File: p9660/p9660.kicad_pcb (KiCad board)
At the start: 2 copper layers, 58 x 51 mm, 6 parts, among them J1 Conn_02x08_Counter_Clockwise, J2 Conn_02x08_Counter_Clockwise, J3 Conn_02x08_Counter_Clockwise, J4 Conn_02x08_Counter_Clockwise, J5 Conn_02x04_Counter_Clockwise

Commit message: done for realz?
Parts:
- added REF**: balls, Hayden Crimes:balls, B.Cu at (70.4, 47.7)
- added TP1: TestPoint, TestPoint:TestPoint_Pad_2.0x2.0mm, F.Cu at (42.0, 31.0)
- added TP2: TestPoint, TestPoint:TestPoint_Pad_2.0x2.0mm, F.Cu at (42.0, 78.0)
- added TP3: TestPoint, TestPoint:TestPoint_Pad_2.0x2.0mm, F.Cu at (96.0, 78.0)
- added TP4: TestPoint, TestPoint:TestPoint_Pad_2.0x2.0mm, F.Cu at (96.0, 31.0)
- added TP5: TestPoint, TestPoint:TestPoint_Pad_2.0x2.0mm, F.Cu at (63.0, 31.0)
- added TP6: TestPoint, TestPoint:TestPoint_Pad_2.0x2.0mm, F.Cu at (62.0, 78.0)
- added TP7: TestPoint, TestPoint:TestPoint_Pad_2.0x2.0mm, F.Cu at (75.0, 31.0)
- added TP8: TestPoint, TestPoint:TestPoint_Pad_2.0x2.0mm, F.Cu at (76.0, 78.0)
- moved J5 2.04 mm to (73.0, 75.5)
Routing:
- net CK1-: track 36.2 -> 38.2 mm
- net CK1+: track 36.3 -> 38.3 mm
- net CK2+: track 24.2 -> 26.3 mm
- net CK2-: track 24.3 -> 26.4 mm
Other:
- board text added: "github.com/hadn69/P9660-Breakout"

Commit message: Update p9660.kicad_pcb
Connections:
- C1 pad 3: D3 -> GND
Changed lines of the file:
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@@
 		)
 		(property "Value" "~"
-			(at -3 2 270)
+			(at -3 2 -90)
 			(unlocked yes)
 			(layer "F.Fab")
@@
 			(layer "F.SilkS")
 		)
-		(pad "1" thru_hole circle
-			(at 1.045 0.63 270)
-			(size 1.22 1.22)
-			(drill 0.71)
-			(layers "*.Cu" "*.Mask")
-			(remove_unused_layers no)
-			(net 2 "GND")
-			(pinfunction "GND")
-			(pintype "input")
-		)
-		(pad "1" thru_hole circle
+		(pad "" np_thru_hole circle
 			(at 1.045 2.35 270)
 			(size 0.84 0.84)
 			(drill 0.84)
-			(property pad_prop_heatsink)
-			(layers "*.Cu" "*.Mask")
-			(remove_unused_layers no)
+			(layers "F&B.Cu" "*.Mask")
 			(pinfunction "GND")
 			(pintype "input")
@@
 				(prefer_zone_connections no)
 			)
+		)
+		(pad "1" thru_hole circle
+			(at 1.045 0.63 270)
+			(size 1.22 1.22)
+			(drill 0.71)
+			(layers "*.Cu" "*.Mask")
+			(remove_unused_layers no)
+			(net 2 "GND")
+			(pinfunction "GND")
+			(pintype "input")
 		)
 		(pad "1" smd oval
@@
 			(property pad_prop_bga)
 			(layers "F.Cu" "F.Paste" "F.Mask")
-			(net 13 "D3")
+			(net 2 "GND")
 			(pinfunction "D3")
 			(pintype "input")

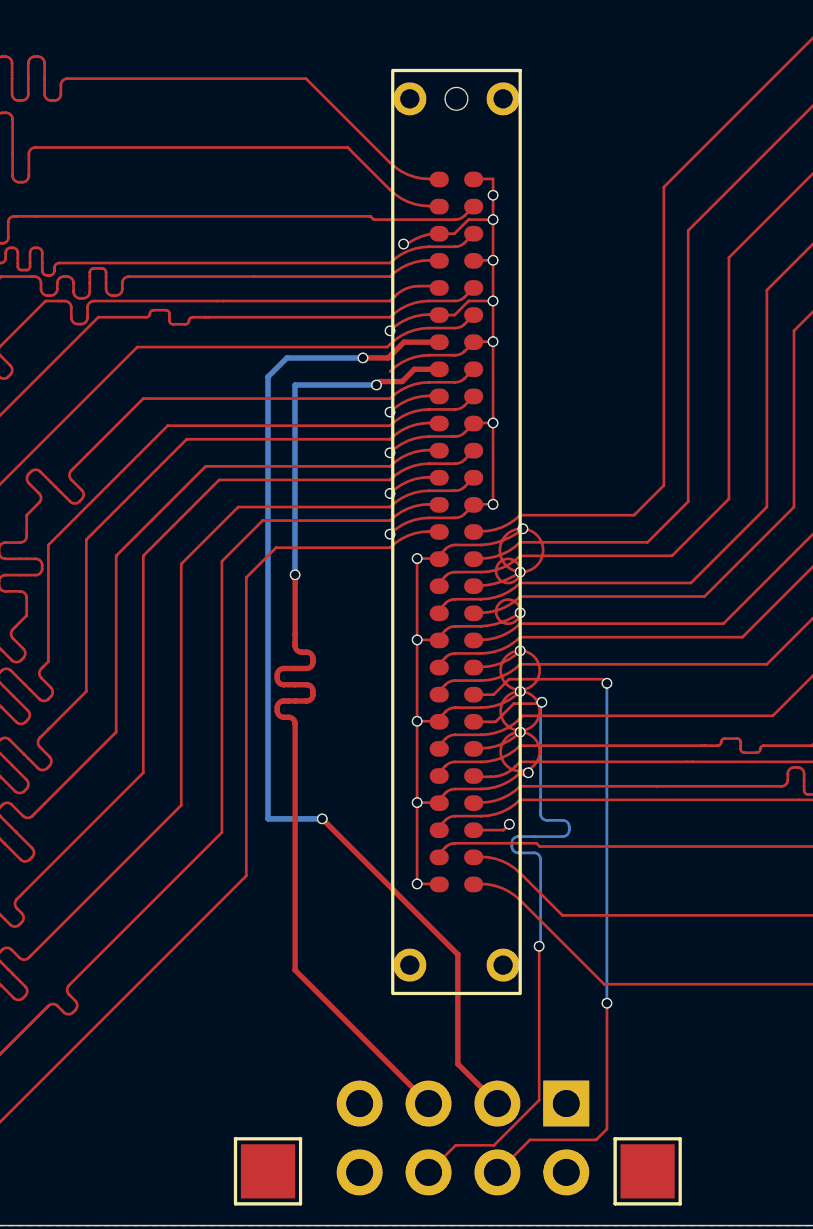
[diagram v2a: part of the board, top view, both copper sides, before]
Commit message: added renders + followed keepout better
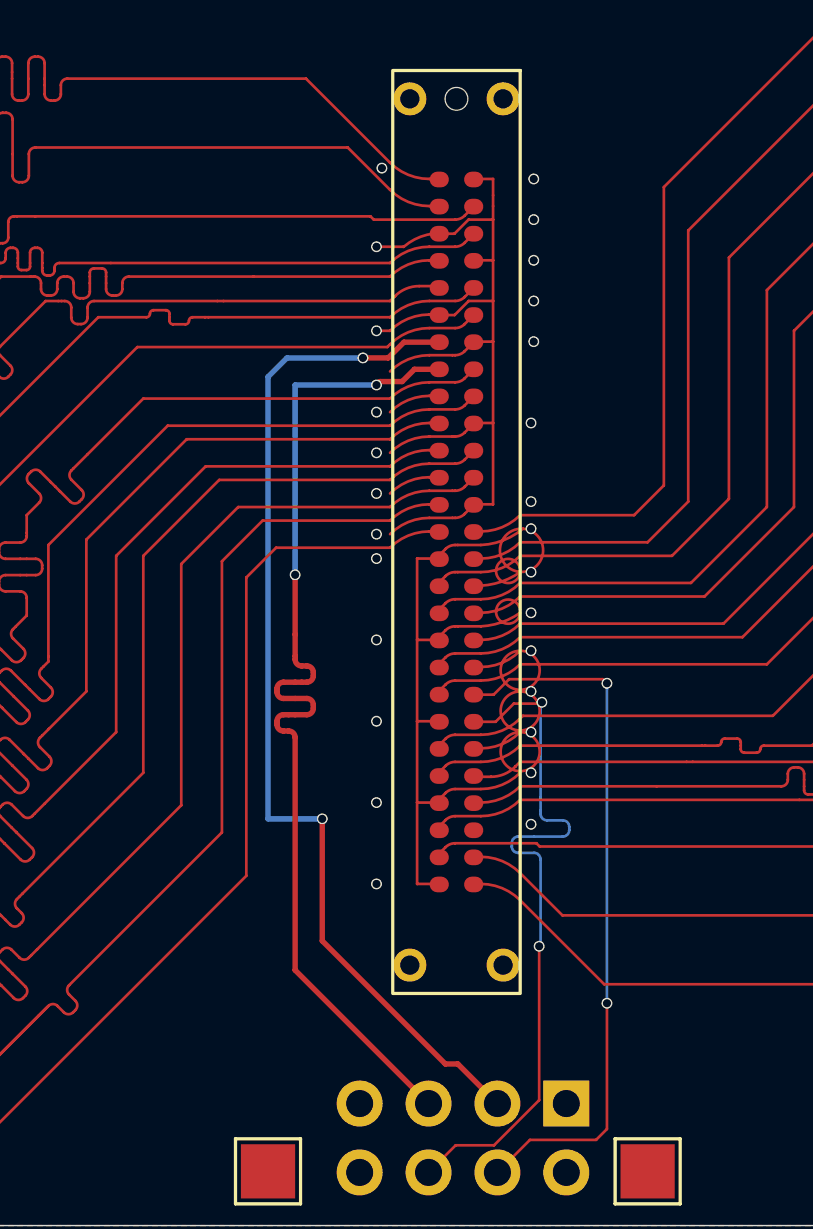
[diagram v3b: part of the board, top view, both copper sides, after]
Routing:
- net GND: track 157.7 -> 153.5 mm, vias 26 -> 27
